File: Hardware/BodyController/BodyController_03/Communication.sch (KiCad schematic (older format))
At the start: 14 parts, among them U16 MCP2562-H/SN, U29 FT230X

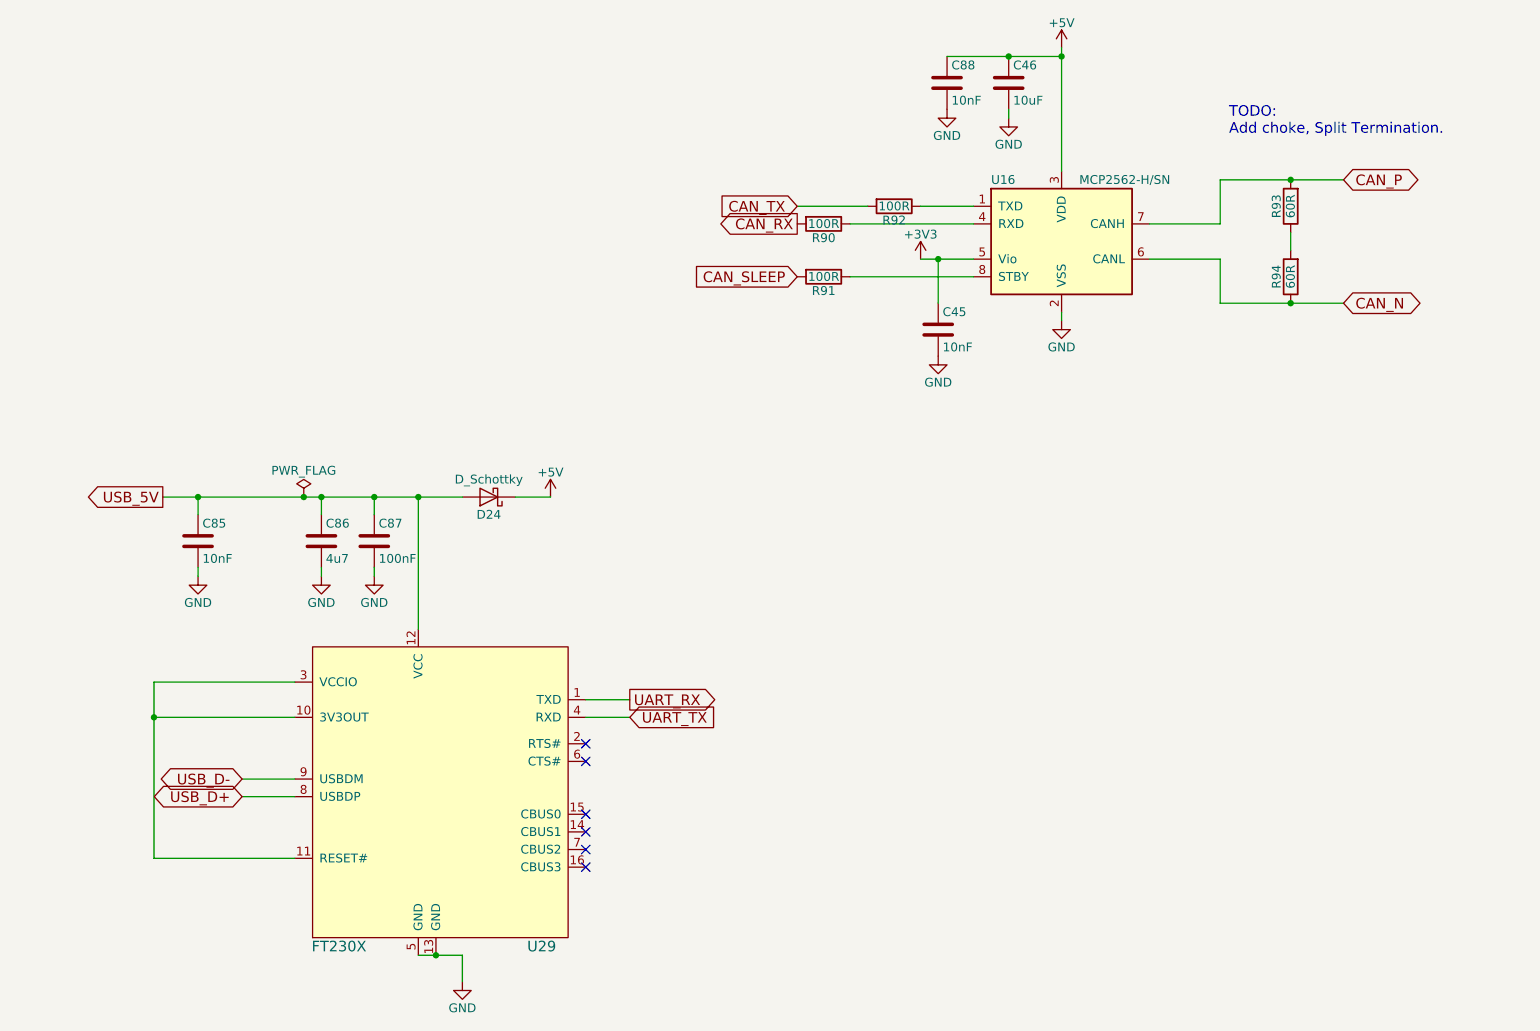
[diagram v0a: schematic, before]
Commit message: Body Controller Layout Done
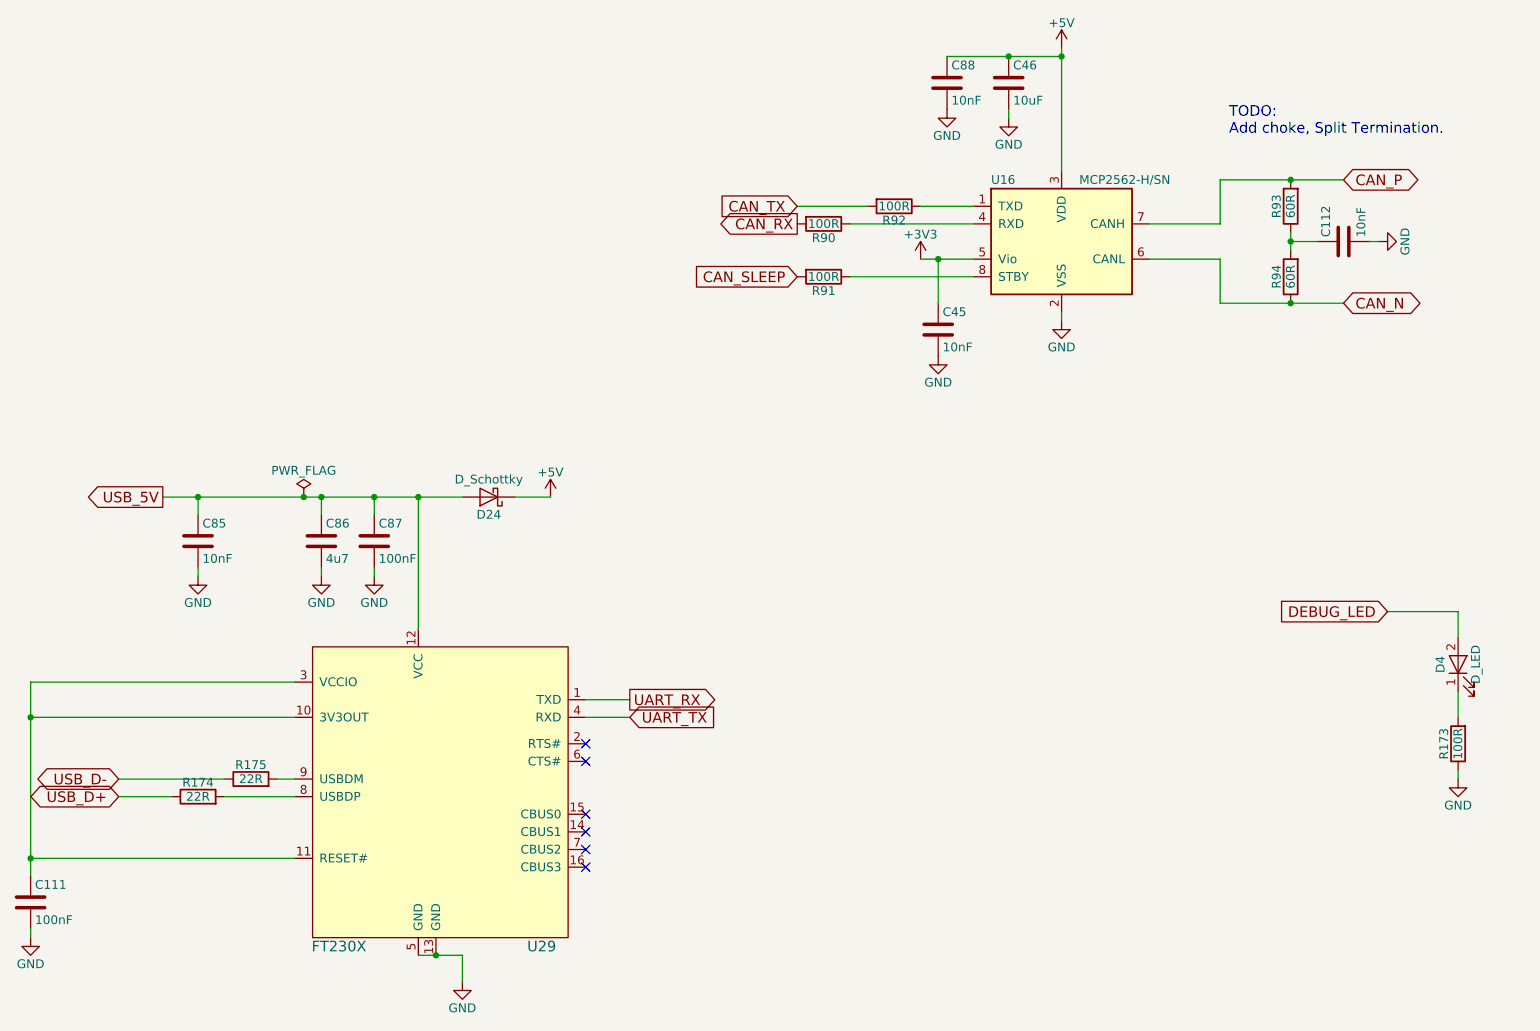
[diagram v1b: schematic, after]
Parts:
- added C111: 100nF, Capacitors_SMD:C_0603, symbol C
- added C112: 10nF, Capacitors_SMD:C_0603, symbol C
- added D4: D_LED, Diodes_SMD:D_0603, symbol LED
- added R173: 100R, Resistors_SMD:R_0603, symbol R
- added R174, R175: 22R, Resistors_SMD:R_0603, symbol R
- U16: PartNumber (none) -> MCP2562-H/SN
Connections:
- net GND: now also C111.2, C112.2, R173.1
- net USB_D+: now also R174.1; no longer U29.8 (USBDP)
- net USB_D-: now also R175.1; no longer U29.9 (USBDM)
- net at R93.1, R94.2: now also C112.1
- net at U29.10 (3V3OUT), U29.11 (RESET#), U29.3 (VCCIO): now also C111.1
- new net: R174.2, U29.8 (USBDP)
- new net: R175.2, U29.9 (USBDM)
- new net: D4.1 (K), R173.2
- new net DEBUG_LED: D4.2 (A)
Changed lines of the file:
@@
 LIBS:ICs
 LIBS:Connectors
+LIBS:microchip_dspic33dsc
+LIBS:switches
 LIBS:BodyController_03-cache
 EELAYER 25 0
@@
 $Descr A4 11693 8268
 encoding utf-8
-Sheet 9 12
+Sheet 9 13
 Title ""
 Date ""
@@
 F 2 "Housings_SOIC:SOIC-8_3.9x4.9mm_Pitch1.27mm" H 7450 2100 50  0001 C CIN
 F 3 "" H 7450 2600 50  0001 C CNN
+F 4 "MCP2562-H/SN" H 0   0   50  0001 C CNN "PartNumber"
 	1    7450 2600
 	1    0    0    -1
 $EndComp
 $Comp
-L GND #PWR0117
+L GND #PWR0140
 U 1 1 59956B61
 P 7450 3050
-F 0 "#PWR0117" H 7450 2800 50  0001 C CNN
+F 0 "#PWR0140" H 7450 2800 50  0001 C CNN
 F 1 "GND" H 7450 2900 50  0000 C CNN
 F 2 "" H 7450 3050 50  0001 C CNN
@@
 $EndComp
 $Comp
-L +5V #PWR0118
+L +5V #PWR0141
 U 1 1 59956B7A
 P 7450 1500
-F 0 "#PWR0118" H 7450 1350 50  0001 C CNN
+F 0 "#PWR0141" H 7450 1350 50  0001 C CNN
 F 1 "+5V" H 7450 1640 50  0000 C CNN
 F 2 "" H 7450 1500 50  0001 C CNN
@@
 $EndComp
 $Comp
-L GND #PWR0119
+L GND #PWR0142
 U 1 1 59956BCC
 P 7150 1900
-F 0 "#PWR0119" H 7150 1650 50  0001 C CNN
+F 0 "#PWR0142" H 7150 1650 50  0001 C CNN
 F 1 "GND" H 7150 1750 50  0000 C CNN
 F 2 "" H 7150 1900 50  0001 C CNN
@@
 $EndComp
 $Comp
-L GND #PWR0120
+L GND #PWR0143
 U 1 1 59956F85
 P 6750 3250
-F 0 "#PWR0120" H 6750 3000 50  0001 C CNN
+F 0 "#PWR0143" H 6750 3000 50  0001 C CNN
 F 1 "GND" H 6750 3100 50  0000 C CNN
 F 2 "" H 6750 3250 50  0001 C CNN
@@
 $EndComp
 $Comp
-L +3V3 #PWR0121
+L +3V3 #PWR0144
 U 1 1 59956FC4
 P 6650 2700
-F 0 "#PWR0121" H 6650 2550 50  0001 C CNN
+F 0 "#PWR0144" H 6650 2550 50  0001 C CNN
 F 1 "+3V3" H 6650 2840 50  0000 C CNN
 F 2 "" H 6650 2700 50  0001 C CNN
@@
 $EndComp
 $Comp
-L GND #PWR0122
+L GND #PWR0145
 U 1 1 59A84C78
 P 3550 4500
-F 0 "#PWR0122" H 3550 4250 50  0001 C CNN
+F 0 "#PWR0145" H 3550 4250 50  0001 C CNN
 F 1 "GND" H 3550 4350 50  0000 C CNN
 F 2 "" H 3550 4500 50  0001 C CNN
@@
 $EndComp
 $Comp
-L GND #PWR0123
+L GND #PWR0146
 U 1 1 59A84CA7
 P 3250 4500
-F 0 "#PWR0123" H 3250 4250 50  0001 C CNN
+F 0 "#PWR0146" H 3250 4250 50  0001 C CNN
 F 1 "GND" H 3250 4350 50  0000 C CNN
 F 2 "" H 3250 4500 50  0001 C CNN
@@
 $EndComp
 $Comp
-L GND #PWR0124
+L GND #PWR0147
 U 1 1 59A84D2D
 P 2550 4500
-F 0 "#PWR0124" H 2550 4250 50  0001 C CNN
+F 0 "#PWR0147" H 2550 4250 50  0001 C CNN
 F 1 "GND" H 2550 4350 50  0000 C CNN
 F 2 "" H 2550 4500 50  0001 C CNN
@@
 $EndComp
 $Comp
-L +5V #PWR0125
+L +5V #PWR0148
 U 1 1 59A85952
 P 4550 4050
-F 0 "#PWR0125" H 4550 3900 50  0001 C CNN
+F 0 "#PWR0148" H 4550 3900 50  0001 C CNN
 F 1 "+5V" H 4550 4190 50  0000 C CNN
 F 2 "" H 4550 4050 50  0001 C CNN
@@
 $EndComp
 $Comp
-L GND #PWR0126
+L GND #PWR0149
 U 1 1 59A86CDB
 P 4050 6800
-F 0 "#PWR0126" H 4050 6550 50  0001 C CNN
+F 0 "#PWR0149" H 4050 6550 50  0001 C CNN
 F 1 "GND" H 4050 6650 50  0000 C CNN
 F 2 "" H 4050 6800 50  0001 C CNN
@@
 $EndComp
 $Comp
-L PWR_FLAG #FLG0127
+L PWR_FLAG #FLG0150
 U 1 1 59A88735
 P 3150 4050
-F 0 "#FLG0127" H 3150 4125 50  0001 C CNN
+F 0 "#FLG0150" H 3150 4125 50  0001 C CNN
 F 1 "PWR_FLAG" H 3150 4200 50  0000 C CNN
 F 2 "" H 3150 4050 50  0001 C CNN
@@
 $EndComp
 $Comp
-L GND #PWR0128
+L GND #PWR0151
 U 1 1 59A895F5
 P 6800 1850
-F 0 "#PWR0128" H 6800 1600 50  0001 C CNN
+F 0 "#PWR0151" H 6800 1600 50  0001 C CNN
 F 1 "GND" H 6800 1700 50  0000 C CNN
 F 2 "" H 6800 1850 50  0001 C CNN
@@
 	1    6800 1850
 	1    0    0    -1
+$EndComp
+$Comp
+L C C111
+U 1 1 5A45C0D4
+P 1600 6350
+F 0 "C111" H 1625 6450 50  0000 L CNN
+F 1 "100nF" H 1625 6250 50  0000 L CNN
+F 2 "Capacitors_SMD:C_0603" H 1638 6200 50  0001 C CNN
+F 3 "https://product.tdk.com/info/en/documents/chara_sheet/CGA3E2X7R1H104K080AA.pdf" H 1600 6350 50  0001 C CNN
+F 4 "CGA3E2X7R1H104K080AA" H -1950 2050 50  0001 C CNN "PartNumber"
+	1    1600 6350
+	1    0    0    -1
+$EndComp
+$Comp
+L GND #PWR0152
+U 1 1 5A45C122
+P 1600 6550
+F 0 "#PWR0152" H 1600 6300 50  0001 C CNN
+F 1 "GND" H 1600 6400 50  0000 C CNN
+F 2 "" H 1600 6550 50  0001 C CNN
+F 3 "" H 1600 6550 50  0001 C CNN
+	1    1600 6550
+	1    0    0    -1
+$EndComp
+$Comp
+L LED D4
+U 1 1 5A45CB14
+P 9700 5000
+F 0 "D4" H 9700 5100 50  0000 C CNN
+F 1 "D_LED" H 9700 4900 50  0000 C CNN
+F 2 "Diodes_SMD:D_0603" H 9700 5000 50  0001 C CNN
+F 3 "http://optoelectronics.liteon.com/upload/download/DS22-2000-223/LTST-C191KRKT.PDF" H 9700 5000 50  0001 C CNN
+F 4 "LTST-C191KRKT" H 0   0   50  0001 C CNN "PartNumber"
+	1    9700 5000
+	0    -1   -1   0
+$EndComp
+$Comp
+L R R173
+U 1 1 5A45CC59
+P 9700 5450
+F 0 "R173" V 9780 5450 50  0000 C CNN
+F 1 "100R" V 9700 5450 50  0000 C CNN
+F 2 "Resistors_SMD:R_0603" V 9630 5450 50  0001 C CNN
+F 3 "" H 9700 5450 50  0001 C CNN
+	1    9700 5450
+	-1   0    0    1
+$EndComp
+$Comp
+L GND #PWR0153
+U 1 1 5A45CD1A
+P 9700 5650
+F 0 "#PWR0153" H 9700 5400 50  0001 C CNN
+F 1 "GND" H 9700 5500 50  0000 C CNN
+F 2 "" H 9700 5650 50  0001 C CNN
+F 3 "" H 9700 5650 50  0001 C CNN
+	1    9700 5650
+	1    0    0    -1
+$EndComp
+$Comp
+L C C112
+U 1 1 5A45DDEF
+P 9050 2600
+F 0 "C112" H 9075 2700 50  0000 L CNN
+F 1 "10nF" H 9075 2500 50  0000 L CNN
+F 2 "Capacitors_SMD:C_0603" H 9088 2450 50  0001 C CNN
+F 3 "https://product.tdk.com/info/en/documents/chara_sheet/CGA3E2X7R1H103K080AA.pdf" H 9050 2600 50  0001 C CNN
+F 4 "CGA3E2X7R1H103K080AA" H 6500 -1700 50  0001 C CNN "PartNumber"
+	1    9050 2600
+	0    -1   -1   0
+$EndComp
+$Comp
+L GND #PWR0154
+U 1 1 5A45DDF5
+P 9250 2600
+F 0 "#PWR0154" H 9250 2350 50  0001 C CNN
+F 1 "GND" H 9250 2450 50  0000 C CNN
+F 2 "" H 9250 2600 50  0001 C CNN
+F 3 "" H 9250 2600 50  0001 C CNN
+	1    9250 2600
+	0    -1   -1   0
+$EndComp
+$Comp
+L R R175
+U 1 1 5A45ECCD
+P 2850 5650
+F 0 "R175" V 2930 5650 50  0000 C CNN
+F 1 "22R" V 2850 5650 50  0000 C CNN
+F 2 "Resistors_SMD:R_0603" V 2780 5650 50  0001 C CNN
+F 3 "" H 2850 5650 50  0001 C CNN
+	1    2850 5650
+	0    -1   -1   0
+$EndComp
+$Comp
+L R R174
+U 1 1 5A45EF18
+P 2550 5750
+F 0 "R174" V 2630 5750 50  0000 C CNN
+F 1 "22R" V 2550 5750 50  0000 C CNN
+F 2 "Resistors_SMD:R_0603" V 2480 5750 50  0001 C CNN
+F 3 "" H 2550 5750 50  0001 C CNN
+	1    2550 5750
+	0    -1   -1   0
 $EndComp
 Text GLabel 9050 2250 2    60   BiDi ~ 0
@@
 Text GLabel 2350 4050 0    60   Output ~ 0
 USB_5V
-Text GLabel 2800 5750 0    60   BiDi ~ 0
+Text GLabel 2100 5750 0    60   BiDi ~ 0
 USB_D+
-Text GLabel 2800 5650 0    60   BiDi ~ 0
+Text GLabel 2100 5650 0    60   BiDi ~ 0
 USB_D-
 Text GLabel 5000 5200 2    60   Output ~ 0
@@
 Text GLabel 5000 5300 2    60   Input ~ 0
 UART_TX
+Text GLabel 9300 4700 0    60   Input ~ 0
+DEBUG_LED
 Wire Wire Line
 	7450 3050 7450 3000
@@
 	5950 2400 6350 2400
 Wire Wire Line
-	3100 5650 2800 5650
-Wire Wire Line
-	3100 5750 2800 5750
-Wire Wire Line
 	3800 4050 3800 4800
 Wire Wire Line
@@
 	4550 4050 4350 4050
 Wire Wire Line
-	3100 5100 2300 5100
-Wire Wire Line
-	2300 5100 2300 6100
-Wire Wire Line
-	2300 5300 3100 5300
-Wire Wire Line
-	2300 6100 3100 6100
+	3100 5100 1600 5100
+Wire Wire Line
+	1600 5100 1600 6200
+Wire Wire Line
+	1600 5300 3100 5300
+Wire Wire Line
+	1600 6100 3100 6100
 Wire Wire Line
 	5000 5300 4750 5300
@@
 Wire Wire Line
 	3800 6650 4050 6650
+Wire Wire Line
+	1600 6550 1600 6500
+Wire Wire Line
+	9700 5650 9700 5600
+Wire Wire Line
+	9700 5300 9700 5150
+Wire Wire Line
+	9300 4700 9700 4700
+Wire Wire Line
+	9700 4700 9700 4850
+Wire Wire Line
+	9250 2600 9200 2600
+Wire Wire Line
+	8900 2600 8750 2600
+Wire Wire Line
+	3100 5650 3000 5650
+Wire Wire Line
+	2700 5650 2100 5650
+Wire Wire Line
+	2100 5750 2400 5750
+Wire Wire Line
+	2700 5750 3100 5750
 Connection ~ 7450 1550
 Connection ~ 8750 2250
@@
 Connection ~ 3250 4050
 Connection ~ 3800 4050
-Connection ~ 2300 5300
+Connection ~ 1600 5300
 Connection ~ 3900 6650
 Connection ~ 3150 4050
 Connection ~ 7150 1550
 Connection ~ 6750 2700
+Connection ~ 1600 6100
+Connection ~ 8750 2600
 NoConn ~ 4750 5450
 NoConn ~ 4750 5550

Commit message: Added resistor values via BOM importer. Changed layout file to add large CAN resistors and buffer to 1.65V Reference
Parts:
- R173, R90, R91, R92: PartNumber (none) -> AC0603FR-07100RL
- R174, R175: PartNumber (none) -> AC0603FR-0722RL
- R93, R94: footprint Resistors_SMD:R_0603 -> Resistors_SMD:R_2512; PartNumber (none) -> RMCF2512JT62R0
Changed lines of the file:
@@
 EESchema Schematic File Version 2
+LIBS:BodyController_03-rescue
 LIBS:power
 LIBS:device
@@
 $EndComp
 $Comp
-L GND #PWR151
+L GND #PWR0146
 U 1 1 59956B61
 P 7450 3050
-F 0 "#PWR151" H 7450 2800 50  0001 C CNN
+F 0 "#PWR0146" H 7450 2800 50  0001 C CNN
 F 1 "GND" H 7450 2900 50  0000 C CNN
 F 2 "" H 7450 3050 50  0001 C CNN
@@
 $EndComp
 $Comp
-L +5V #PWR150
+L +5V #PWR0147
 U 1 1 59956B7A
 P 7450 1500
-F 0 "#PWR150" H 7450 1350 50  0001 C CNN
+F 0 "#PWR0147" H 7450 1350 50  0001 C CNN
 F 1 "+5V" H 7450 1640 50  0000 C CNN
 F 2 "" H 7450 1500 50  0001 C CNN
@@
 $EndComp
 $Comp
-L GND #PWR149
+L GND #PWR0148
 U 1 1 59956BCC
 P 7150 1900
-F 0 "#PWR149" H 7150 1650 50  0001 C CNN
+F 0 "#PWR0148" H 7150 1650 50  0001 C CNN
 F 1 "GND" H 7150 1750 50  0000 C CNN
 F 2 "" H 7150 1900 50  0001 C CNN
@@
 F 1 "100R" V 6500 2400 50  0000 C CNN
 F 2 "Resistors_SMD:R_0603" V 6430 2400 50  0001 C CNN
-F 3 "" H 6500 2400 50  0001 C CNN
+F 3 "http://www.yageo.com/NewPortal/yageodocoutput?fileName=/pdf/R-Chip/PYu-AC_51_RoHS_L_6.pdf" H 6500 2400 50  0001 C CNN
+F 4 "AC0603FR-07100RL" H 0   0   50  0001 C CNN "PartNumber"
 	1    6500 2400
 	0    1    1    0
@@
 F 1 "100R" V 6100 2500 50  0000 C CNN
 F 2 "Resistors_SMD:R_0603" V 6030 2500 50  0001 C CNN
-F 3 "" H 6100 2500 50  0001 C CNN
+F 3 "http://www.yageo.com/NewPortal/yageodocoutput?fileName=/pdf/R-Chip/PYu-AC_51_RoHS_L_6.pdf" H 6100 2500 50  0001 C CNN
+F 4 "AC0603FR-07100RL" H 0   0   50  0001 C CNN "PartNumber"
 	1    6100 2500
 	0    1    1    0
@@
 F 1 "100R" V 6100 2800 50  0000 C CNN
 F 2 "Resistors_SMD:R_0603" V 6030 2800 50  0001 C CNN
-F 3 "" H 6100 2800 50  0001 C CNN
+F 3 "http://www.yageo.com/NewPortal/yageodocoutput?fileName=/pdf/R-Chip/PYu-AC_51_RoHS_L_6.pdf" H 6100 2800 50  0001 C CNN
+F 4 "AC0603FR-07100RL" H 0   0   50  0001 C CNN "PartNumber"
 	1    6100 2800
 	0    1    1    0
@@
 F 0 "R93" V 8830 2400 50  0000 C CNN
 F 1 "60R" V 8750 2400 50  0000 C CNN
-F 2 "Resistors_SMD:R_0603" V 8680 2400 50  0001 C CNN
-F 3 "" H 8750 2400 50  0001 C CNN
+F 2 "Resistors_SMD:R_2512" V 8680 2400 50  0001 C CNN
+F 3 "https://www.seielect.com/Catalog/SEI-RMCF_RMCP.pdf" H 8750 2400 50  0001 C CNN
+F 4 "RMCF2512JT62R0" V 8750 2400 60  0001 C CNN "PartNumber"
 	1    8750 2400
 	-1   0    0    1
@@
 F 0 "R94" V 8830 2800 50  0000 C CNN
 F 1 "60R" V 8750 2800 50  0000 C CNN
-F 2 "Resistors_SMD:R_0603" V 8680 2800 50  0001 C CNN
-F 3 "" H 8750 2800 50  0001 C CNN
+F 2 "Resistors_SMD:R_2512" V 8680 2800 50  0001 C CNN
+F 3 "https://www.seielect.com/Catalog/SEI-RMCF_RMCP.pdf" H 8750 2800 50  0001 C CNN
+F 4 "RMCF2512JT62R0" V 8750 2800 60  0001 C CNN "PartNumber"
 	1    8750 2800
 	-1   0    0    1
@@
 $EndComp
 $Comp
-L GND #PWR147
+L GND #PWR0149
 U 1 1 59956F85
 P 6750 3250
-F 0 "#PWR147" H 6750 3000 50  0001 C CNN
+F 0 "#PWR0149" H 6750 3000 50  0001 C CNN
 F 1 "GND" H 6750 3100 50  0000 C CNN
 F 2 "" H 6750 3250 50  0001 C CNN
@@
 $EndComp
 $Comp
-L +3V3 #PWR146
+L +3V3 #PWR0150
 U 1 1 59956FC4
 P 6650 2700
-F 0 "#PWR146" H 6650 2550 50  0001 C CNN
+F 0 "#PWR0150" H 6650 2550 50  0001 C CNN
 F 1 "+3V3" H 6650 2840 50  0000 C CNN
 F 2 "" H 6650 2700 50  0001 C CNN
@@
 $EndComp
 $Comp
-L GND #PWR143
+L GND #PWR0151
 U 1 1 59A84C78
 P 3550 4500
-F 0 "#PWR143" H 3550 4250 50  0001 C CNN
+F 0 "#PWR0151" H 3550 4250 50  0001 C CNN
 F 1 "GND" H 3550 4350 50  0000 C CNN
 F 2 "" H 3550 4500 50  0001 C CNN
@@
 $EndComp
 $Comp
-L GND #PWR142
+L GND #PWR0152
 U 1 1 59A84CA7
 P 3250 4500
-F 0 "#PWR142" H 3250 4250 50  0001 C CNN
+F 0 "#PWR0152" H 3250 4250 50  0001 C CNN
 F 1 "GND" H 3250 4350 50  0000 C CNN
 F 2 "" H 3250 4500 50  0001 C CNN
@@
 $EndComp
 $Comp
-L GND #PWR141
+L GND #PWR0153
 U 1 1 59A84D2D
 P 2550 4500
-F 0 "#PWR141" H 2550 4250 50  0001 C CNN
+F 0 "#PWR0153" H 2550 4250 50  0001 C CNN
 F 1 "GND" H 2550 4350 50  0000 C CNN
 F 2 "" H 2550 4500 50  0001 C CNN
@@
 $EndComp
 $Comp
-L +5V #PWR145
+L +5V #PWR0154
 U 1 1 59A85952
 P 4550 4050
-F 0 "#PWR145" H 4550 3900 50  0001 C CNN
+F 0 "#PWR0154" H 4550 3900 50  0001 C CNN
 F 1 "+5V" H 4550 4190 50  0000 C CNN
 F 2 "" H 4550 4050 50  0001 C CNN
@@
 $EndComp
 $Comp
-L GND #PWR144
+L GND #PWR0155
 U 1 1 59A86CDB
 P 4050 6800
-F 0 "#PWR144" H 4050 6550 50  0001 C CNN
+F 0 "#PWR0155" H 4050 6550 50  0001 C CNN
 F 1 "GND" H 4050 6650 50  0000 C CNN
 F 2 "" H 4050 6800 50  0001 C CNN
@@
 $EndComp
 $Comp
-L PWR_FLAG #FLG5
+L PWR_FLAG #FLG0156
 U 1 1 59A88735
 P 3150 4050
-F 0 "#FLG5" H 3150 4125 50  0001 C CNN
+F 0 "#FLG0156" H 3150 4125 50  0001 C CNN
 F 1 "PWR_FLAG" H 3150 4200 50  0000 C CNN
 F 2 "" H 3150 4050 50  0001 C CNN
@@
 $EndComp
 $Comp
-L GND #PWR148
+L GND #PWR0157
 U 1 1 59A895F5
 P 6800 1850
-F 0 "#PWR148" H 6800 1600 50  0001 C CNN
+F 0 "#PWR0157" H 6800 1600 50  0001 C CNN
 F 1 "GND" H 6800 1700 50  0000 C CNN
 F 2 "" H 6800 1850 50  0001 C CNN
@@
 $EndComp
 $Comp
-L GND #PWR140
+L GND #PWR0158
 U 1 1 5A45C122
 P 1600 6550
-F 0 "#PWR140" H 1600 6300 50  0001 C CNN
+F 0 "#PWR0158" H 1600 6300 50  0001 C CNN
 F 1 "GND" H 1600 6400 50  0000 C CNN
 F 2 "" H 1600 6550 50  0001 C CNN
@@
 F 1 "100R" V 9700 5450 50  0000 C CNN
 F 2 "Resistors_SMD:R_0603" V 9630 5450 50  0001 C CNN
-F 3 "" H 9700 5450 50  0001 C CNN
+F 3 "http://www.yageo.com/NewPortal/yageodocoutput?fileName=/pdf/R-Chip/PYu-AC_51_RoHS_L_6.pdf" H 9700 5450 50  0001 C CNN
+F 4 "AC0603FR-07100RL" H 0   0   50  0001 C CNN "PartNumber"
 	1    9700 5450
 	-1   0    0    1
 $EndComp
 $Comp
-L GND #PWR153
+L GND #PWR0159
 U 1 1 5A45CD1A
 P 9700 5650
-F 0 "#PWR153" H 9700 5400 50  0001 C CNN
+F 0 "#PWR0159" H 9700 5400 50  0001 C CNN
 F 1 "GND" H 9700 5500 50  0000 C CNN
 F 2 "" H 9700 5650 50  0001 C CNN
@@
 $EndComp
 $Comp
-L GND #PWR152
+L GND #PWR0160
 U 1 1 5A45DDF5
 P 9250 2600
-F 0 "#PWR152" H 9250 2350 50  0001 C CNN
+F 0 "#PWR0160" H 9250 2350 50  0001 C CNN
 F 1 "GND" H 9250 2450 50  0000 C CNN
 F 2 "" H 9250 2600 50  0001 C CNN
@@
 F 1 "22R" V 2850 5650 50  0000 C CNN
 F 2 "Resistors_SMD:R_0603" V 2780 5650 50  0001 C CNN
-F 3 "" H 2850 5650 50  0001 C CNN
+F 3 "http://www.yageo.com/NewPortal/yageodocoutput?fileName=/pdf/R-Chip/PYu-AC_51_RoHS_L_6.pdf" H 2850 5650 50  0001 C CNN
+F 4 "AC0603FR-0722RL" H 0   0   50  0001 C CNN "PartNumber"
 	1    2850 5650
 	0    -1   -1   0
@@
 F 1 "22R" V 2550 5750 50  0000 C CNN
 F 2 "Resistors_SMD:R_0603" V 2480 5750 50  0001 C CNN
-F 3 "" H 2550 5750 50  0001 C CNN
+F 3 "http://www.yageo.com/NewPortal/yageodocoutput?fileName=/pdf/R-Chip/PYu-AC_51_RoHS_L_6.pdf" H 2550 5750 50  0001 C CNN
+F 4 "AC0603FR-0722RL" H 0   0   50  0001 C CNN "PartNumber"
 	1    2550 5750
 	0    -1   -1   0
